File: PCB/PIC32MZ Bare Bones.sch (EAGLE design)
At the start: 40 parts, among them U1 PIC32MZ2048EC(G/H/M)144-PL, U2 ADP3338AKCZ-3.3, X1 24MHz, Abracon ABM8, X2 32.768kHz, X3 USB-MICROB, X4 USB-A-SMD

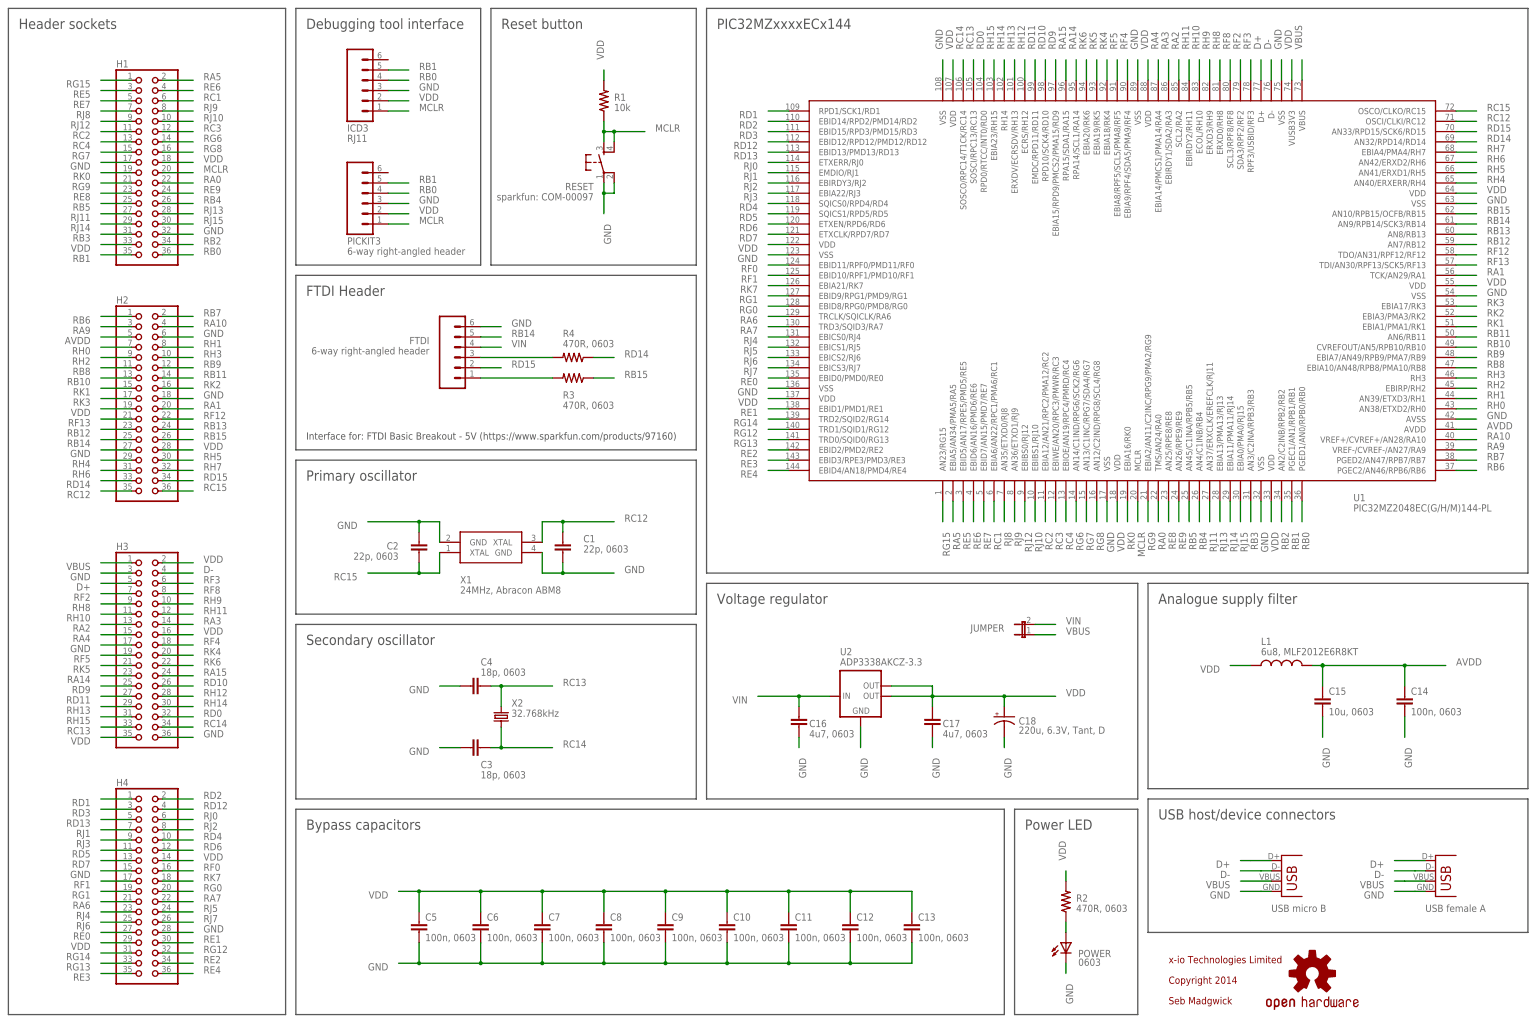
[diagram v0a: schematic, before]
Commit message: Change some component value and part numbers
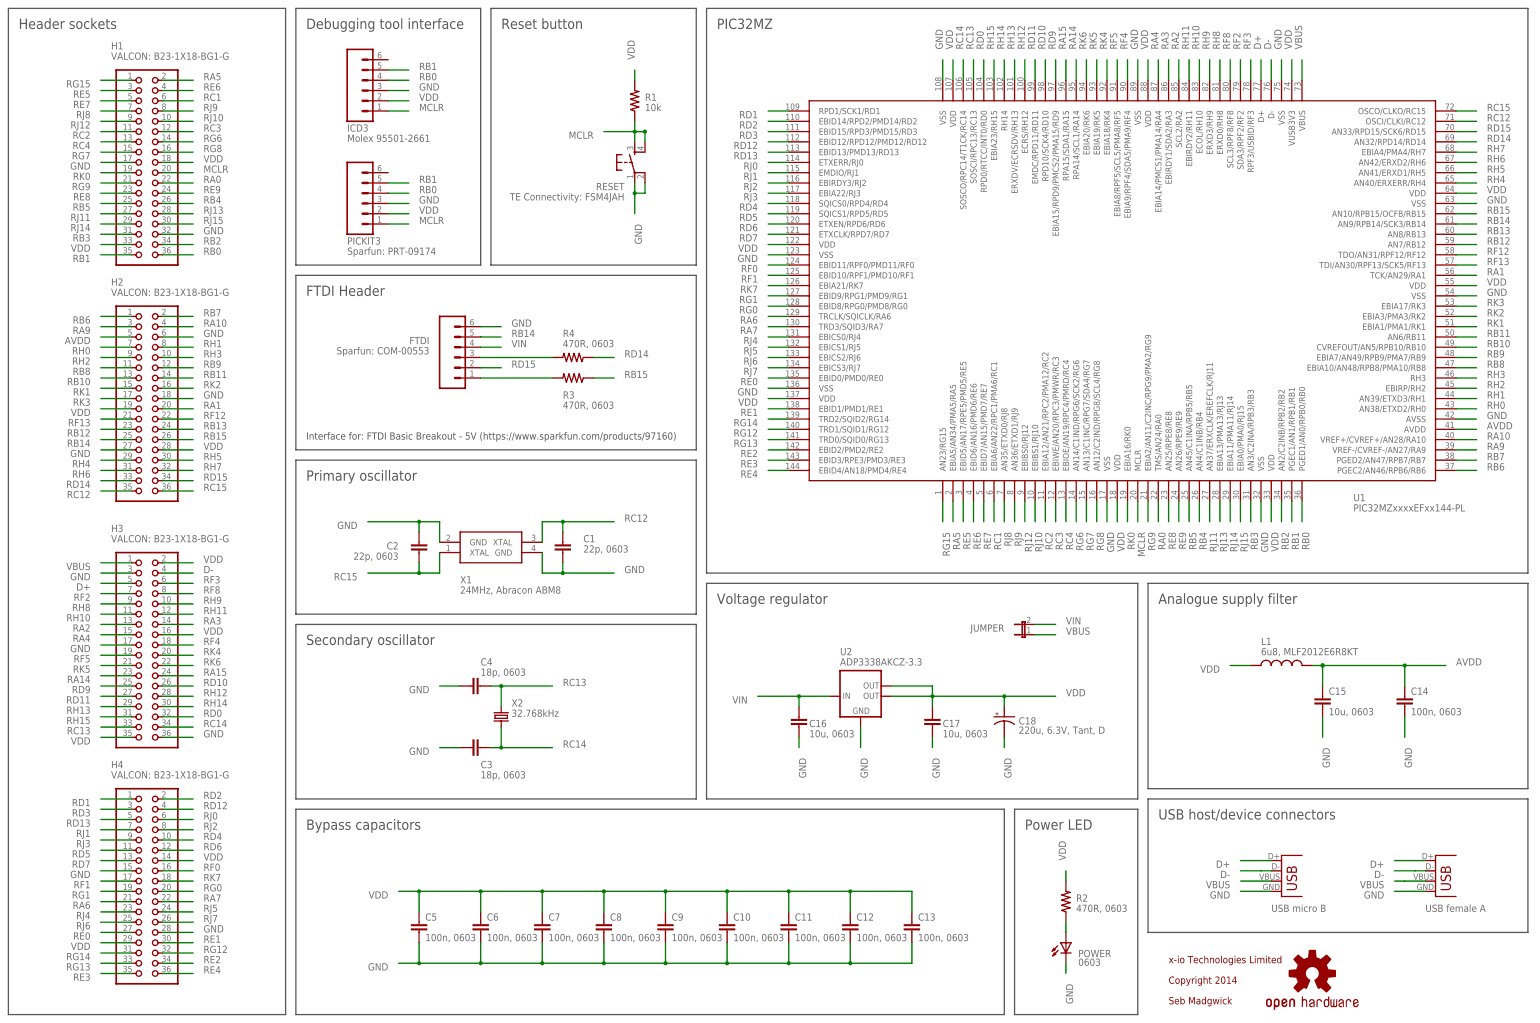
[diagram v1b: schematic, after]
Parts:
- C16, C17: value 4u7, 0603 -> 10u, 0603
- FTDI: value 6-way right-angled header -> Sparfun: COM-00553
- H1, H2, H3, H4: value (none) -> VALCON: B23-1X18-BG1-G
- ICD3: value RJ11 -> Molex 95501-2661
- PICKIT3: value 6-way right-angled header -> Sparfun: PRT-09174
- RESET: value sparkfun: COM-00097 -> TE Connectivity: FSM4JAH
- U1: value PIC32MZ2048EC(G/H/M)144-PL -> PIC32MZxxxxEFxx144-PL
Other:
- note added: "PIC32MZ"
- note removed: "PIC32MZxxxxECx144"
- moved on the sheet: R1, RESET
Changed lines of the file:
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@@
 </classes>
 <parts>
-<part name="U1" library="x-io" deviceset="PIC32MZ2048EC(G/H/M)144" device="-PL"/>
+<part name="U1" library="x-io" deviceset="PIC32MZ2048EC(G/H/M)144" device="-PL" value="PIC32MZxxxxEFxx144-PL"/>
 <part name="FRAME1" library="frames" deviceset="A3L-LOC" device=""/>
-<part name="H1" library="pinhead" deviceset="PINHD-2X18" device=""/>
-<part name="H2" library="pinhead" deviceset="PINHD-2X18" device=""/>
-<part name="H3" library="pinhead" deviceset="PINHD-2X18" device=""/>
-<part name="H4" library="pinhead" deviceset="PINHD-2X18" device=""/>
+<part name="H1" library="pinhead" deviceset="PINHD-2X18" device="" value="VALCON: B23-1X18-BG1-G"/>
+<part name="H2" library="pinhead" deviceset="PINHD-2X18" device="" value="VALCON: B23-1X18-BG1-G"/>
+<part name="H3" library="pinhead" deviceset="PINHD-2X18" device="" value="VALCON: B23-1X18-BG1-G"/>
+<part name="H4" library="pinhead" deviceset="PINHD-2X18" device="" value="VALCON: B23-1X18-BG1-G"/>
 <part name="X1" library="x-io" deviceset="ABM8" device="" value="24MHz, Abracon ABM8"/>
 <part name="C1" library="SparkFun" deviceset="CAP" device="0603-CAP" value="22p, 0603"/>
@@
 <part name="C3" library="SparkFun" deviceset="CAP" device="0603-CAP" value="18p, 0603"/>
 <part name="C4" library="SparkFun" deviceset="CAP" device="0603-CAP" value="18p, 0603"/>
-<part name="ICD3" library="SparkFun" deviceset="RJ11-6" device="PTH" value="RJ11"/>
+<part name="ICD3" library="SparkFun" deviceset="RJ11-6" device="PTH" value="Molex 95501-2661"/>
 <part name="C5" library="SparkFun" deviceset="CAP" device="0603-CAP" value="100n, 0603"/>
 <part name="C6" library="SparkFun" deviceset="CAP" device="0603-CAP" value="100n, 0603"/>
@@
 <part name="L1" library="SparkFun" deviceset="INDUCTOR" device="1007" value="6u8, MLF2012E6R8KT"/>
 <part name="C15" library="SparkFun" deviceset="CAP" device="0603-CAP" value="10u, 0603"/>
-<part name="RESET" library="SparkFun" deviceset="TAC_SWITCH" device="PTH" value="sparkfun: COM-00097"/>
+<part name="RESET" library="SparkFun" deviceset="TAC_SWITCH" device="PTH" value="TE Connectivity: FSM4JAH"/>
 <part name="R1" library="SparkFun" deviceset="RESISTOR" device="0603-RES" value="10k"/>
-<part name="FTDI" library="SparkFun" deviceset="M06" device="SIP" value="6-way right-angled header"/>
+<part name="FTDI" library="SparkFun" deviceset="M06" device="SIP" value="Sparfun: COM-00553"/>
 <part name="POWER" library="SparkFun" deviceset="LED" device="0603" value="0603"/>
 <part name="R2" library="SparkFun" deviceset="RESISTOR" device="0603-RES" value="470R, 0603"/>
 <part name="U2" library="x-io" deviceset="ADP3338" device="" value="ADP3338AKCZ-3.3"/>
-<part name="C16" library="SparkFun" deviceset="CAP" device="0603-CAP" value="4u7, 0603"/>
-<part name="C17" library="SparkFun" deviceset="CAP" device="0603-CAP" value="4u7, 0603"/>
+<part name="C16" library="SparkFun" deviceset="CAP" device="0603-CAP" value="10u, 0603"/>
+<part name="C17" library="SparkFun" deviceset="CAP" device="0603-CAP" value="10u, 0603"/>
 <part name="C18" library="rcl" deviceset="CPOL-US" device="SMCD" value="220u, 6.3V, Tant, D"/>
 <part name="JUMPER" library="SparkFun" deviceset="JUMPER-2" device="SMD-NO"/>
-<part name="PICKIT3" library="SparkFun" deviceset="M06" device="SIP" value="6-way right-angled header"/>
+<part name="PICKIT3" library="SparkFun" deviceset="M06" device="SIP" value="Sparfun: PRT-09174"/>
 <part name="U$4" library="SparkFun_08_2011" deviceset="OSHW-LOGO" device="S"/>
 <part name="X3" library="SparkFun" deviceset="USB" device="-MICROB"/>
@@
 <wire x1="177.8" y1="114.3" x2="381" y2="114.3" width="0.1524" layer="97"/>
 <wire x1="381" y1="114.3" x2="381" y2="254" width="0.1524" layer="97"/>
-<text x="180.34" y="248.92" size="2.54" layer="97">PIC32MZxxxxECx144</text>
+<text x="180.34" y="248.92" size="2.54" layer="97">PIC32MZ</text>
 <wire x1="76.2" y1="254" x2="121.92" y2="254" width="0.1524" layer="97"/>
 <wire x1="121.92" y1="254" x2="121.92" y2="190.5" width="0.1524" layer="97"/>
@@
 </instance>
 <instance part="FRAME1" gate="G$1" x="0" y="0"/>
-<instance part="H1" gate="A" x="38.1" y="215.9"/>
-<instance part="H2" gate="A" x="38.1" y="157.48"/>
-<instance part="H3" gate="A" x="38.1" y="96.52"/>
-<instance part="H4" gate="A" x="38.1" y="38.1"/>
+<instance part="H1" gate="A" x="38.1" y="215.9" smashed="yes">
+<attribute name="NAME" x="30.48" y="243.84" size="1.778" layer="95"/>
+<attribute name="VALUE" x="30.48" y="241.3" size="1.778" layer="96"/>
+</instance>
+<instance part="H2" gate="A" x="38.1" y="157.48" smashed="yes">
+<attribute name="NAME" x="30.48" y="185.42" size="1.778" layer="95"/>
+<attribute name="VALUE" x="30.48" y="182.88" size="1.778" layer="96"/>
+</instance>
+<instance part="H3" gate="A" x="38.1" y="96.52" smashed="yes">
+<attribute name="NAME" x="30.48" y="124.46" size="1.778" layer="95"/>
+<attribute name="VALUE" x="30.48" y="121.92" size="1.778" layer="96"/>
+</instance>
+<instance part="H4" gate="A" x="38.1" y="38.1" smashed="yes">
+<attribute name="NAME" x="30.48" y="66.04" size="1.778" layer="95"/>
+<attribute name="VALUE" x="30.48" y="63.5" size="1.778" layer="96"/>
+</instance>
 <instance part="X1" gate="G$1" x="124.46" y="119.38" smashed="yes">
 <attribute name="NAME" x="116.84" y="111.76" size="1.778" layer="95"/>
@@
 </instance>
 <instance part="C15" gate="G$1" x="330.2" y="81.28"/>
-<instance part="RESET" gate="S" x="152.4" y="215.9" smashed="yes" rot="R90">
-<attribute name="NAME" x="149.86" y="210.82" size="1.778" layer="95" rot="R180"/>
-<attribute name="VALUE" x="149.86" y="208.28" size="1.778" layer="96" rot="R180"/>
-</instance>
-<instance part="R1" gate="G$1" x="152.4" y="231.14" smashed="yes" rot="R90">
-<attribute name="NAME" x="154.94" y="231.14" size="1.778" layer="95"/>
-<attribute name="VALUE" x="154.94" y="228.6" size="1.778" layer="96"/>
+<instance part="RESET" gate="S" x="160.02" y="215.9" smashed="yes" rot="R90">
+<attribute name="NAME" x="157.48" y="210.82" size="1.778" layer="95" rot="R180"/>
+<attribute name="VALUE" x="157.48" y="208.28" size="1.778" layer="96" rot="R180"/>
+</instance>
+<instance part="R1" gate="G$1" x="160.02" y="231.14" smashed="yes" rot="R90">
+<attribute name="NAME" x="162.56" y="231.14" size="1.778" layer="95"/>
+<attribute name="VALUE" x="162.56" y="228.6" size="1.778" layer="96"/>
 </instance>
 <instance part="FTDI" gate="G$1" x="116.84" y="167.64" smashed="yes">
@@
 <segment>
 <pinref part="R1" gate="G$1" pin="2"/>
-<wire x1="152.4" y1="236.22" x2="152.4" y2="238.76" width="0.1524" layer="91"/>
-<label x="152.4" y="241.3" size="1.778" layer="95" rot="R90"/>
+<wire x1="160.02" y1="236.22" x2="160.02" y2="238.76" width="0.1524" layer="91"/>
+<label x="160.02" y="241.3" size="1.778" layer="95" rot="R90"/>
 </segment>
 <segment>
@@
 <segment>
 <pinref part="RESET" gate="S" pin="3"/>
-<wire x1="152.4" y1="220.98" x2="152.4" y2="223.52" width="0.1524" layer="91"/>
+<wire x1="160.02" y1="220.98" x2="160.02" y2="223.52" width="0.1524" layer="91"/>
 <pinref part="RESET" gate="S" pin="4"/>
-<wire x1="152.4" y1="223.52" x2="152.4" y2="226.06" width="0.1524" layer="91"/>
-<wire x1="152.4" y1="223.52" x2="154.94" y2="223.52" width="0.1524" layer="91"/>
-<wire x1="154.94" y1="223.52" x2="154.94" y2="220.98" width="0.1524" layer="91"/>
-<junction x="152.4" y="223.52"/>
-<wire x1="154.94" y1="223.52" x2="162.56" y2="223.52" width="0.1524" layer="91"/>
-<junction x="154.94" y="223.52"/>
+<wire x1="160.02" y1="223.52" x2="160.02" y2="226.06" width="0.1524" layer="91"/>
+<wire x1="160.02" y1="223.52" x2="162.56" y2="223.52" width="0.1524" layer="91"/>
+<wire x1="162.56" y1="223.52" x2="162.56" y2="220.98" width="0.1524" layer="91"/>
+<junction x="160.02" y="223.52"/>
+<wire x1="162.56" y1="223.52" x2="152.4" y2="223.52" width="0.1524" layer="91"/>
+<junction x="162.56" y="223.52"/>
 <pinref part="R1" gate="G$1" pin="1"/>
-<label x="165.1" y="223.52" size="1.778" layer="95"/>
+<label x="149.86" y="223.52" size="1.778" layer="95" rot="R180"/>
 </segment>
 <segment>
@@
 <segment>
 <pinref part="RESET" gate="S" pin="1"/>
-<wire x1="152.4" y1="210.82" x2="152.4" y2="208.28" width="0.1524" layer="91"/>
+<wire x1="160.02" y1="210.82" x2="160.02" y2="208.28" width="0.1524" layer="91"/>
 <pinref part="RESET" gate="S" pin="2"/>
-<wire x1="152.4" y1="208.28" x2="152.4" y2="203.2" width="0.1524" layer="91"/>
-<wire x1="152.4" y1="208.28" x2="154.94" y2="208.28" width="0.1524" layer="91"/>
-<wire x1="154.94" y1="208.28" x2="154.94" y2="210.82" width="0.1524" layer="91"/>
-<junction x="152.4" y="208.28"/>
-<label x="152.4" y="200.66" size="1.778" layer="95" rot="R270"/>
-</segment>
-<segment>
+<wire x1="160.02" y1="208.28" x2="160.02" y2="203.2" width="0.1524" layer="91"/>
+<wire x1="160.02" y1="208.28" x2="162.56" y2="208.28" width="0.1524" layer="91"/>
+<wire x1="162.56" y1="208.28" x2="162.56" y2="210.82" width="0.1524" layer="91"/>
+<junction x="160.02" y="208.28"/>
+<label x="160.02" y="200.66" size="1.778" layer="95" rot="R270"/>
+</segment>
+<segment>

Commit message: Create Gerbers for v1.2 PCB
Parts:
- U1: value PIC32MZxxxxEFxx144-PL -> PIC32MZxxxxEFx144-PL
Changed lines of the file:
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@@
 </classes>
 <parts>
-<part name="U1" library="x-io" deviceset="PIC32MZ2048EC(G/H/M)144" device="-PL" value="PIC32MZxxxxEFxx144-PL"/>
+<part name="U1" library="x-io" deviceset="PIC32MZ2048EC(G/H/M)144" device="-PL" value="PIC32MZxxxxEFx144-PL"/>
 <part name="FRAME1" library="frames" deviceset="A3L-LOC" device=""/>
 <part name="H1" library="pinhead" deviceset="PINHD-2X18" device="" value="VALCON: B23-1X18-BG1-G"/>
